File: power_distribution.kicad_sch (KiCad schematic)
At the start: 79 parts, among them Q1 PMOS, Q10 2PNP, Q11 2NPN, Q12 PMOS, Q13 2PNP, Q14 2PNP, Q15 2PNP, Q2 PMOS, Q3 2NPN, Q4 PMOS, Q5 PMOS, Q6 PMOS, Q7 PMOS, Q8 2NPN, Q9 PMOS, U1 PAC1954

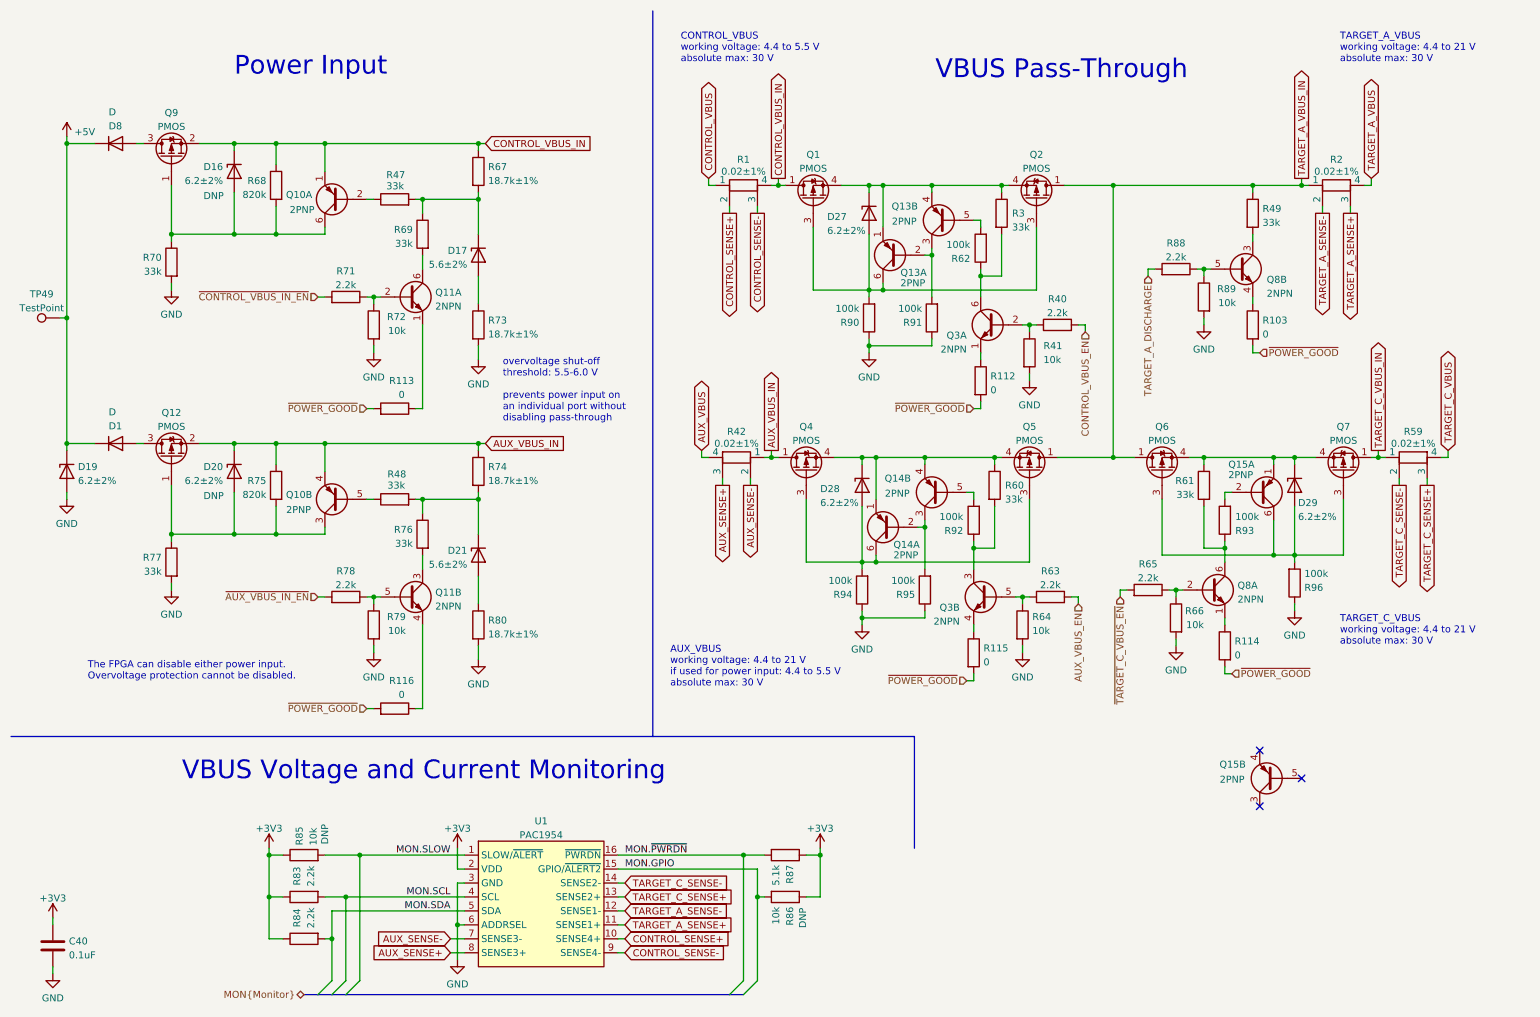
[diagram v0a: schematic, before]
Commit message: add first round of hits on lcsc
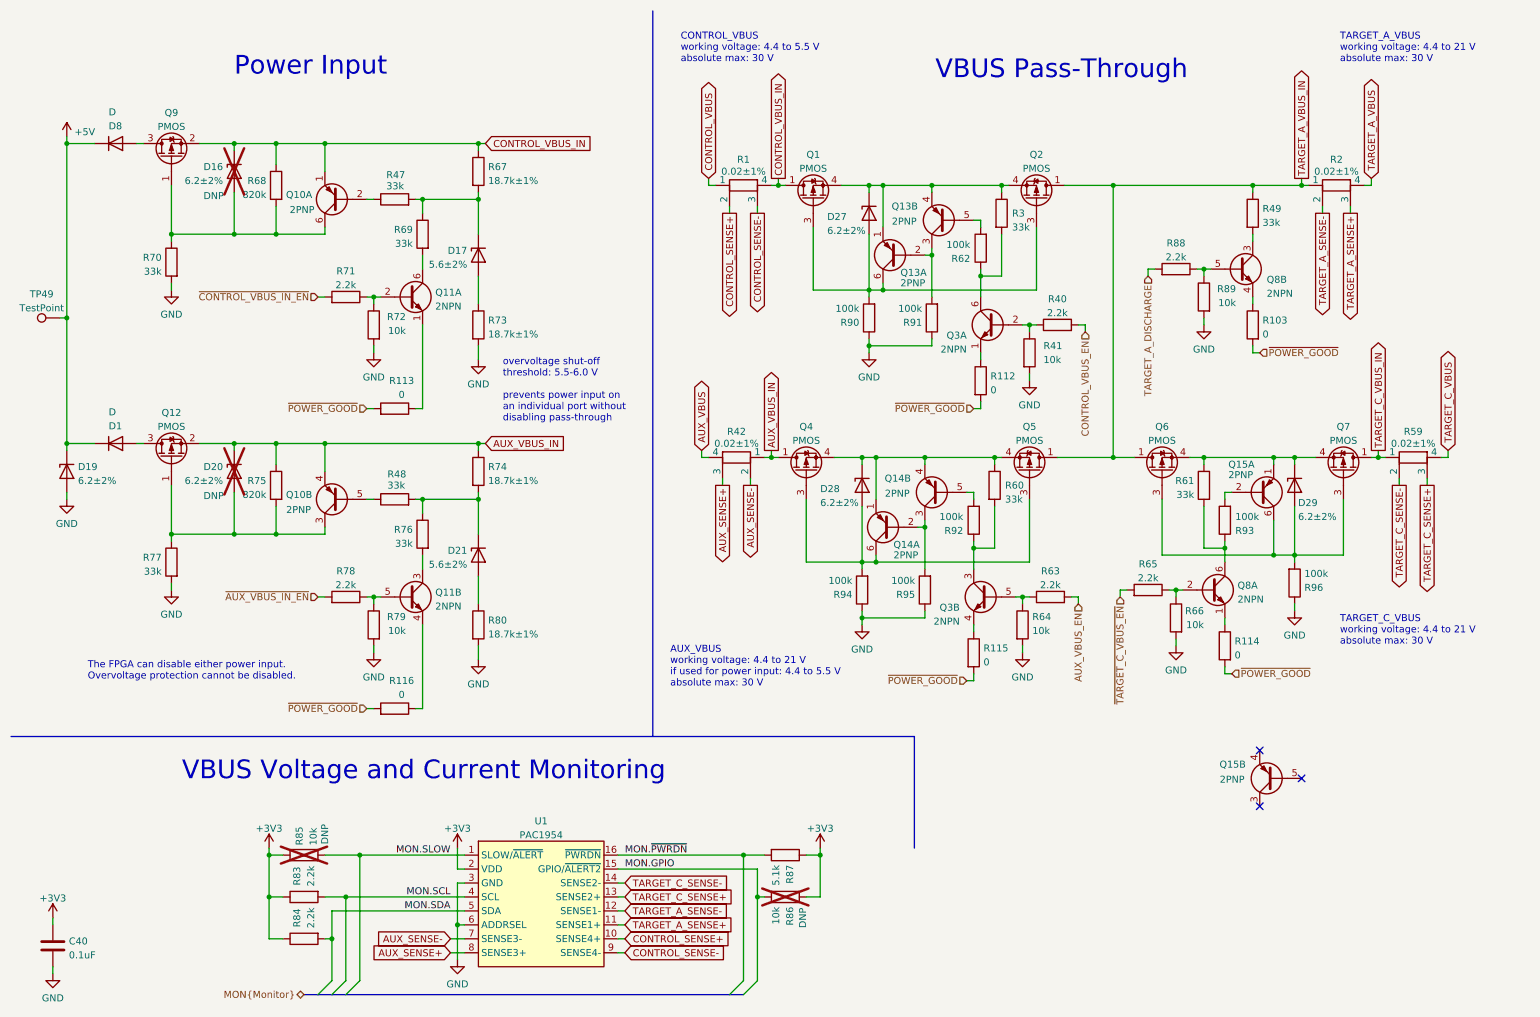
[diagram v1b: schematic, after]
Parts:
- C40: LCSC# (none) -> C100072
- D1, D8: LCSC# (none) -> C6067485
- D16, D20, R85, R86: now not fitted
- D19, D27, D28, D29: LCSC# (none) -> C551211
- Q1, Q2, Q4, Q5, Q6, Q7: LCSC# (none) -> C5377599
- Q10, Q11, Q13, Q14, Q15, Q3, Q8: LCSC# (none) -> C5380687
- Q12, Q9: LCSC# (none) -> C393520
- R103, R112, R113, R114, R115, R116: LCSC# (none) -> C106231
- R40, R63, R65, R71, R78, R83, R84, R88: LCSC# (none) -> C163447
- R41, R64, R66, R72, R79, R89: LCSC# (none) -> C60489
- R62, R90, R91, R92, R93, R94, R95, R96: LCSC# (none) -> C413017
- R68, R75: LCSC# (none) -> C137838
- R87: LCSC# (none) -> C105873
- U1: LCSC# (none) -> C3687526
